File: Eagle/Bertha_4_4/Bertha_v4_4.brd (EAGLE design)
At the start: 100 x 84.6 mm, 115 parts, among them CON1 JACK_DC_BARREL, CON2 JACK_DC_BARREL, IC1 MCP1703DB, J1 RJ12RIGHTANGLE-I2C, J2 RJ12RIGHTANGLE-I2C, Q1 BSP75, Q2 BSP75, Q3 BSP75, Q4 BSP75, Q5 BSP75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

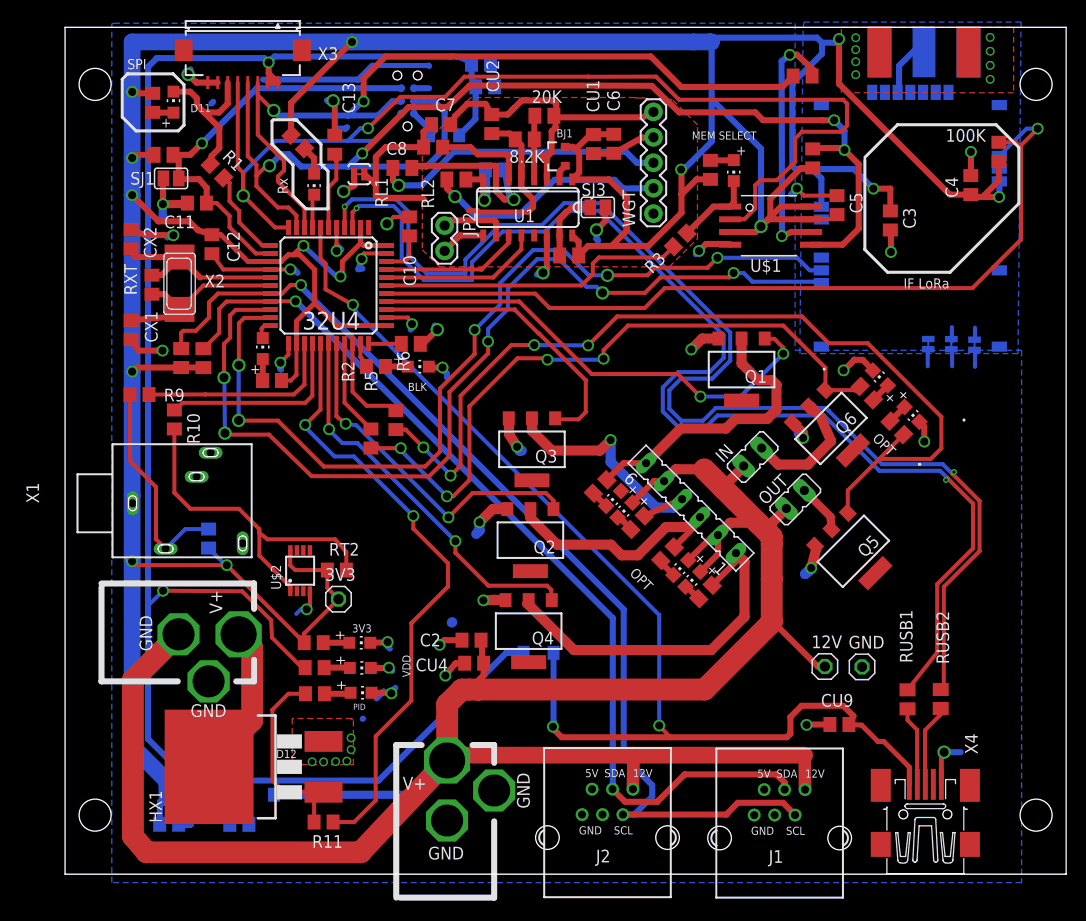
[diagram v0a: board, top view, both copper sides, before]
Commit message: corrected LED error on v4.4, PCB shortened by 1mm
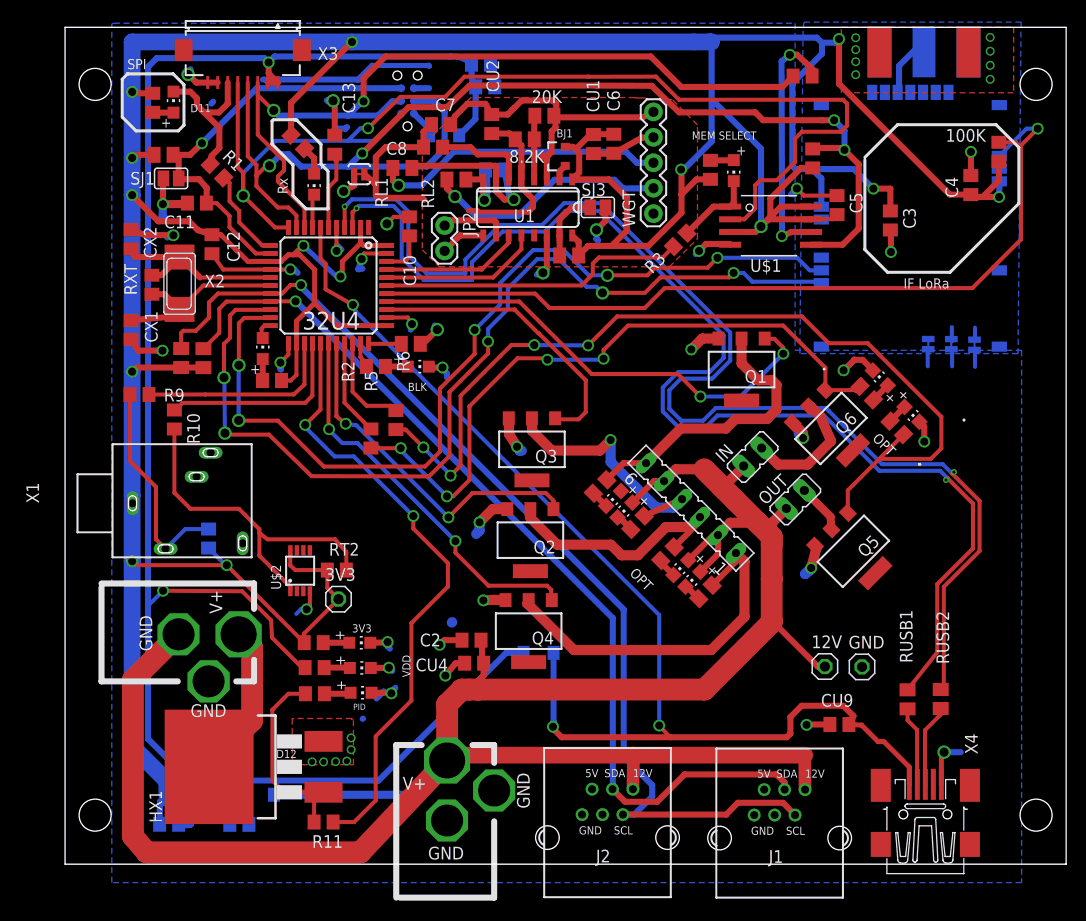
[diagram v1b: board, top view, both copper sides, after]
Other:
- board size 100 x 84.6 mm -> 100 x 83.6 mm
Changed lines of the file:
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@@
 <?xml version="1.0" encoding="utf-8"?>
 <!DOCTYPE eagle SYSTEM "eagle.dtd">
-<eagle version="7.5.0">
+<eagle version="6.5.0">
 <drawing>
 <settings>
@@
 <board>
 <plain>
-<wire x1="-5" y1="-2.9" x2="95" y2="-2.9" width="0" layer="20"/>
-<wire x1="95" y1="-2.9" x2="95" y2="81.7" width="0" layer="20"/>
+<wire x1="-5" y1="-1.9" x2="95" y2="-1.9" width="0" layer="20"/>
+<wire x1="95" y1="-1.9" x2="95" y2="81.7" width="0" layer="20"/>
 <wire x1="95" y1="81.7" x2="-5" y2="81.7" width="0" layer="20"/>
-<wire x1="-5" y1="81.7" x2="-5" y2="-2.9" width="0" layer="20"/>
+<wire x1="-5" y1="81.7" x2="-5" y2="-1.9" width="0" layer="20"/>
 <rectangle x1="42.99585" y1="35.87115" x2="68.98005" y2="35.90925" layer="203" rot="R180"/>
 <rectangle x1="42.99585" y1="35.90925" x2="68.98005" y2="35.94735" layer="203" rot="R180"/>
@@
 <pass name="Default">
 <param name="RoutingGrid" value="6mil"/>
-<param name="AutoGrid" value="1"/>
-<param name="Efforts" value="0"/>
-<param name="TopRouterVariant" value="1"/>
 <param name="tpViaShape" value="round"/>
 <param name="PrefDir.1" value="|"/>

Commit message: changed PID FET part, ref #72
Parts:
- HX1: value IRF3704S -> IPB081N06L3GATMA1
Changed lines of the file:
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@@
 <?xml version="1.0" encoding="utf-8"?>
 <!DOCTYPE eagle SYSTEM "eagle.dtd">
-<eagle version="6.5.0">
+<eagle version="7.5.0">
 <drawing>
 <settings>
@@
 <pass name="Default">
 <param name="RoutingGrid" value="6mil"/>
+<param name="AutoGrid" value="1"/>
+<param name="Efforts" value="0"/>
+<param name="TopRouterVariant" value="1"/>
 <param name="tpViaShape" value="round"/>
 <param name="PrefDir.1" value="|"/>
@@
 </element>
 <element name="RK1" library="resistor" package="M0805" value="10K" x="8.82023125" y="48.6536625" smashed="yes" rot="R90"/>
-<element name="HX1" library="transistor-power" package="D2PACK" value="IRF3704S" x="11.930709375" y="7.823003125" rot="R90"/>
+<element name="HX1" library="transistor-power" package="D2PACK" value="IPB081N06L3GATMA1" x="11.930709375" y="7.823003125" rot="R90"/>
 <element name="R11" library="rcl" package="R0805" value="1K" x="20.826421875" y="2.3096625" smashed="yes" rot="R180">
 <attribute name="NAME" x="22.759665625" y="1.000821875" size="1.27" layer="25" rot="R180"/>

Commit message: correction on PID labelling, closes #71
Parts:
- R11: value 1K -> 10k
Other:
- board text added: "+"
- board text added: "-"
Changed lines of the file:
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@@
 <text x="61.272328125" y="34.7424375" size="0.8128" layer="27" rot="R180">D9</text>
 <text x="64.9194125" y="30.89086875" size="0.8128" layer="27" rot="R180">D8</text>
+<rectangle x1="7.247534375" y1="12.68355625" x2="10.8713" y2="14.38890625" layer="21"/>
+<rectangle x1="1.98951875" y1="19.2207375" x2="3.87245625" y2="23.09330625" layer="21"/>
+<rectangle x1="9.023890625" y1="22.915665625" x2="10.906828125" y2="25.260525" layer="21"/>
+<text x="2.3092625" y="17.231159375" size="1.778" layer="21">+</text>
+<text x="11.652896875" y="23.803871875" size="1.778" layer="21">-</text>
 </plain>
 <attributes>
@@
 </element>
 <element name="RK1" library="resistor" package="M0805" value="10K" x="8.82023125" y="48.6536625" smashed="yes" rot="R90"/>
-<element name="HX1" library="transistor-power" package="D2PACK" value="IPB081N06L3GATMA1" x="11.930709375" y="7.823003125" rot="R90"/>
-<element name="R11" library="rcl" package="R0805" value="1K" x="20.826421875" y="2.3096625" smashed="yes" rot="R180">
+<element name="HX1" library="transistor-power" package="D2PACK" value="IPB081N06L3GATMA1" x="11.930709375" y="7.823003125" smashed="yes" rot="R90">
+<attribute name="NAME" x="4.691709375" y="2.235003125" size="1.27" layer="25" rot="R90"/>
+<attribute name="VALUE" x="15.53734375" y="3.19585625" size="0.8128" layer="27" rot="R90"/>
+</element>
+<element name="R11" library="rcl" package="R0805" value="10k" x="20.826421875" y="2.3096625" smashed="yes" rot="R180">
 <attribute name="NAME" x="22.759665625" y="1.000821875" size="1.27" layer="25" rot="R180"/>
 <attribute name="VALUE" x="21.947165625" y="1.194440625" size="0.8128" layer="27" rot="R180"/>

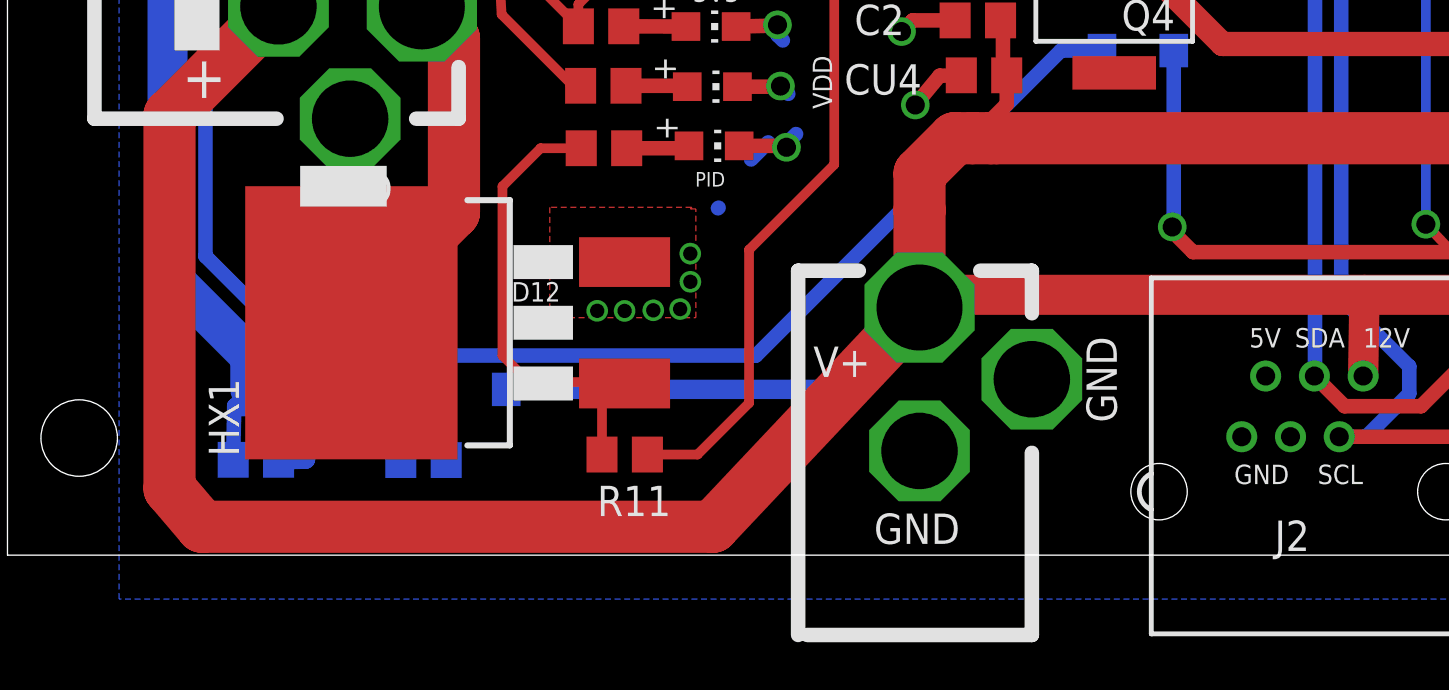
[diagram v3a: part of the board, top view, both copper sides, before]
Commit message: correted PID diode, 4.5 finished, closes #72, ref #47
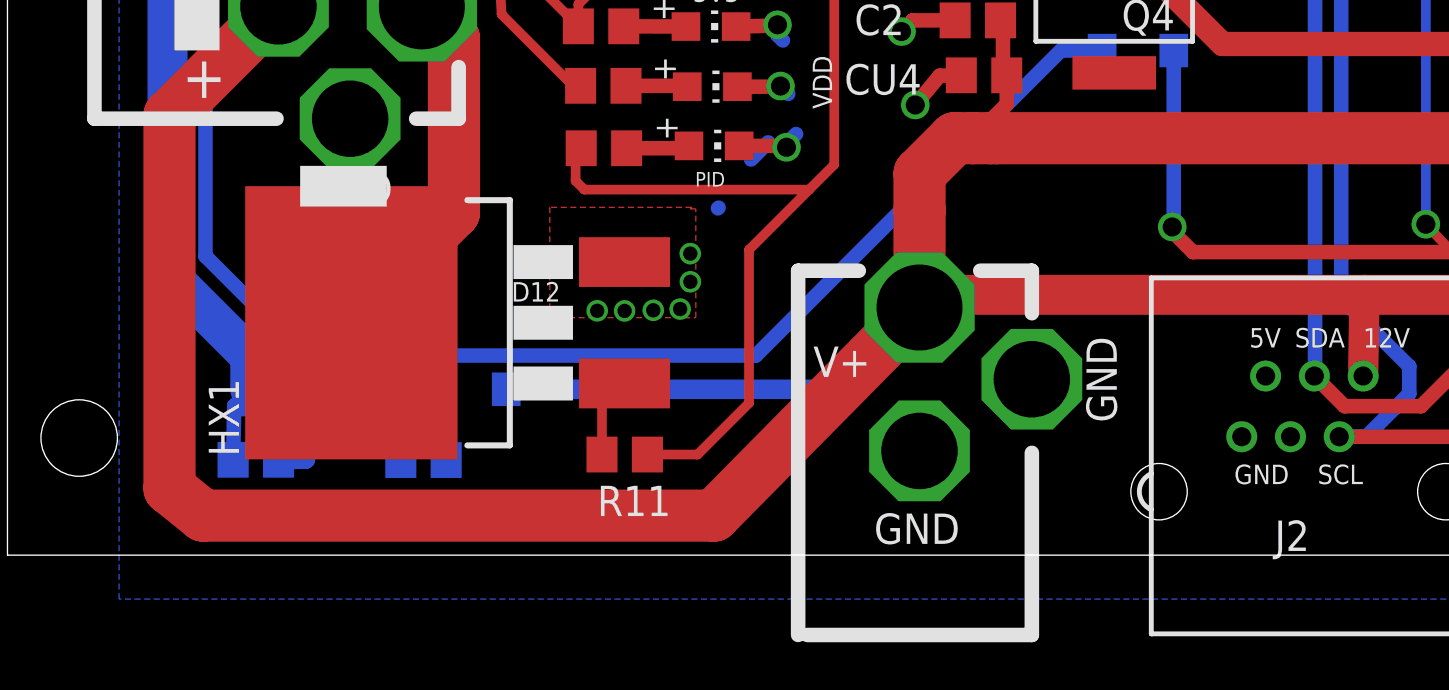
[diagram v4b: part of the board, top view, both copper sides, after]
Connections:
- removed net N$6: HX1.1, R11.2, RK14.2
- new net N$4: HX1.1, R11.2
- net D6*: now also RK14.2
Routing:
- net N$6: track 21.9 -> 0.00 mm
- net D6*: track 61.4 -> 72.8 mm
- net N$4: track 0.00 -> 3.36 mm
- net +12V: track 223.0 -> 222.3 mm
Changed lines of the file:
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@@
 <?xml version="1.0" encoding="utf-8"?>
 <!DOCTYPE eagle SYSTEM "eagle.dtd">
-<eagle version="7.5.0">
+<eagle version="6.5.0">
 <drawing>
 <settings>
@@
 <pass name="Default">
 <param name="RoutingGrid" value="6mil"/>
-<param name="AutoGrid" value="1"/>
-<param name="Efforts" value="0"/>
-<param name="TopRouterVariant" value="1"/>
 <param name="tpViaShape" value="round"/>
 <param name="PrefDir.1" value="|"/>
@@
 <wire x1="17.5042875" y1="57.517396875" x2="17.89638125" y2="57.505253125" width="0.6096" layer="16"/>
 <wire x1="17.89638125" y1="57.505253125" x2="18.23209375" y2="57.169540625" width="0.6096" layer="16"/>
-<wire x1="48.782421875" y1="2.973303125" x2="48.81868125" y2="3.0095625" width="1.016" layer="1"/>
 <wire x1="9.7899125" y1="74.263828125" x2="9.608565625" y2="74.08248125" width="0.6096" layer="16"/>
 <wire x1="22.1147125" y1="61.7076125" x2="22.1147125" y2="59.98025625" width="0.4064" layer="1"/>
@@
 <wire x1="19.139825" y1="23.55973125" x2="18.55165625" y2="23.55973125" width="0.4064" layer="16"/>
 <wire x1="18.55165625" y1="23.55973125" x2="18.090634375" y2="23.098709375" width="0.4064" layer="16"/>
-<wire x1="48.685296875" y1="3.055165625" x2="48.782421875" y2="2.973303125" width="0" layer="19" extent="1-1"/>
 </signal>
 <signal name="SCK">
@@
 <wire x1="23.874015625" y1="2.3096625" x2="26.029196875" y2="4.46484375" width="0.4064" layer="1"/>
 <wire x1="26.029196875" y1="4.46484375" x2="26.029196875" y2="10.87710625" width="0.4064" layer="1"/>
-<wire x1="26.029196875" y1="10.87710625" x2="29.594671875" y2="14.44258125" width="0.4064" layer="1"/>
+<wire x1="26.029196875" y1="10.87710625" x2="28.547415625" y2="13.395325" width="0.4064" layer="1"/>
+<wire x1="28.547415625" y1="13.395325" x2="29.594671875" y2="14.44258125" width="0.4064" layer="1"/>
 <wire x1="29.594671875" y1="14.44258125" x2="29.594671875" y2="22.182609375" width="0.4064" layer="1"/>
 <wire x1="29.594671875" y1="22.182609375" x2="33.244109375" y2="25.832046875" width="0.4064" layer="1"/>
@@
 <wire x1="33.244109375" y1="28.170203125" x2="29.789521875" y2="31.624790625" width="0.4064" layer="1"/>
 <wire x1="29.789521875" y1="31.624790625" x2="29.789521875" y2="32.8806" width="0.4064" layer="1"/>
+<contactref element="RK14" pad="2"/>
+<wire x1="19.008425" y1="15.125984375" x2="18.77176875" y2="14.889328125" width="0.4064" layer="1"/>
+<wire x1="18.77176875" y1="14.889328125" x2="18.77176875" y2="13.7616625" width="0.4064" layer="1"/>
+<wire x1="18.77176875" y1="13.7616625" x2="19.13810625" y2="13.395325" width="0.4064" layer="1"/>
+<wire x1="19.13810625" y1="13.395325" x2="28.547415625" y2="13.395325" width="0.4064" layer="1"/>
 </signal>
 <signal name="D10*">
@@
 <wire x1="29.6659625" y1="5.03755625" x2="29.7030375" y2="5.00048125" width="0.8128" layer="16"/>
 <wire x1="33.16325625" y1="12.641753125" x2="33.16325625" y2="12.529996875" width="0.6096" layer="1"/>
-<wire x1="33.163421875" y1="8.460865625" x2="24.5126" y2="-0.7125125" width="2.1844" layer="1"/>
-<wire x1="24.5126" y1="-0.7125125" x2="3.143890625" y2="-0.7125125" width="2.1844" layer="1"/>
-<wire x1="3.143890625" y1="-0.7125125" x2="1.779190625" y2="0.88968125" width="2.1844" layer="1"/>
+<wire x1="33.163421875" y1="8.460865625" x2="24.559190625" y2="-0.24666875" width="2.1844" layer="1"/>
+<wire x1="24.559190625" y1="-0.24666875" x2="3.19048125" y2="-0.24666875" width="2.1844" layer="1"/>
+<wire x1="3.19048125" y1="-0.24666875" x2="1.779190625" y2="0.88968125" width="2.1844" layer="1"/>
 <wire x1="1.779190625" y1="0.88968125" x2="1.779190625" y2="16.50420625" width="2.1844" layer="1"/>
 <wire x1="36.654575" y1="18.47624375" x2="36.81211875" y2="18.17704375" width="0.8128" layer="1"/>
@@
 <wire x1="9.149803125" y1="65.64509375" x2="9.121325" y2="64.13924375" width="0.6096" layer="1"/>
 </signal>
-<signal name="N$6">
-<contactref element="R11" pad="2"/>
-<contactref element="HX1" pad="1"/>
-<contactref element="RK14" pad="2"/>
-<wire x1="20.46981875" y1="5.02711875" x2="20.820709375" y2="5.283003125" width="0.6096" layer="1"/>
-<wire x1="21.5023" y1="4.814446875" x2="21.301915625" y2="5.01483125" width="0.6096" layer="1"/>
-<wire x1="21.301915625" y1="5.01483125" x2="21.167275" y2="5.01483125" width="0.6096" layer="1"/>
-<wire x1="21.167275" y1="5.01483125" x2="20.48210625" y2="5.01483125" width="0.6096" layer="1"/>
-<wire x1="20.48210625" y1="5.01483125" x2="20.46981875" y2="5.02711875" width="0.6096" layer="1"/>
-<wire x1="21.51950625" y1="5.3670625" x2="21.167275" y2="5.01483125" width="0.6096" layer="1"/>
-<wire x1="19.876421875" y1="2.3096625" x2="19.876421875" y2="4.9727" width="0.4064" layer="1"/>
-<wire x1="19.876421875" y1="4.9727" x2="20.2460375" y2="5.342315625" width="0.4064" layer="1" curve="-90"/>
-<wire x1="20.2460375" y1="5.342315625" x2="20.761396875" y2="5.342315625" width="0.4064" layer="1"/>
-<wire x1="20.761396875" y1="5.342315625" x2="20.820709375" y2="5.283003125" width="0.4064" layer="1" curve="-90"/>
-<wire x1="20.2460375" y1="5.342315625" x2="16.821275" y2="5.342315625" width="0.4064" layer="1"/>
-<wire x1="16.821275" y1="5.342315625" x2="15.710725" y2="6.452865625" width="0.4064" layer="1"/>
-<wire x1="15.710725" y1="6.452865625" x2="15.710725" y2="13.52998125" width="0.4064" layer="1"/>
-<wire x1="15.710725" y1="13.52998125" x2="17.306728125" y2="15.125984375" width="0.4064" layer="1"/>
-<wire x1="17.306728125" y1="15.125984375" x2="19.008425" y2="15.125984375" width="0.4064" layer="1"/>
-</signal>
 <signal name="N$3">
 <contactref element="R2" pad="2"/>
@@
 <wire x1="61.800271875" y1="64.155928125" x2="61.43514375" y2="63.7908" width="0.6096" layer="1"/>
 </signal>
+<signal name="N$4">
+<contactref element="HX1" pad="1"/>
+<contactref element="R11" pad="2"/>
+<wire x1="19.876421875" y1="2.3096625" x2="19.876421875" y2="4.338715625" width="0.4064" layer="1"/>
+<wire x1="19.876421875" y1="4.338715625" x2="20.820709375" y2="5.283003125" width="0.4064" layer="1" curve="-90"/>
+</signal>
 </signals>

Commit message: corrected powerFET labelling
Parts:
- HX1: value IPB081N06L3GATMA1 -> <3V th / 10A
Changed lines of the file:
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@@
 </element>
 <element name="RK1" library="resistor" package="M0805" value="10K" x="8.82023125" y="48.6536625" smashed="yes" rot="R90"/>
-<element name="HX1" library="transistor-power" package="D2PACK" value="IPB081N06L3GATMA1" x="11.930709375" y="7.823003125" smashed="yes" rot="R90">
+<element name="HX1" library="transistor-power" package="D2PACK" value="&lt;3V th / 10A" x="11.930709375" y="7.823003125" smashed="yes" rot="R90">
 <attribute name="NAME" x="4.691709375" y="2.235003125" size="1.27" layer="25" rot="R90"/>
-<attribute name="VALUE" x="15.53734375" y="3.19585625" size="0.8128" layer="27" rot="R90"/>
+<attribute name="VALUE" x="15.57089375" y="3.1623" size="0.8128" layer="27" rot="R90"/>
 </element>
 <element name="R11" library="rcl" package="R0805" value="10k" x="20.826421875" y="2.3096625" smashed="yes" rot="R180">
